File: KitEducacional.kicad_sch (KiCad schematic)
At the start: 23 parts, among them J1 Serial 1, J10 D4, J11 D5, J12 D6, J13 D7, J14 D8, J15 D9, J16 D10, J17 D11, J18 D12, J19 D13, J2 Serial 2, J20 D14, J21 D15, J3 Serial 3, J4 I²C, J5 SPI, J6 D0, J7 D1, J8 D2, J9 D3, U1 ESP32-WROOM-32

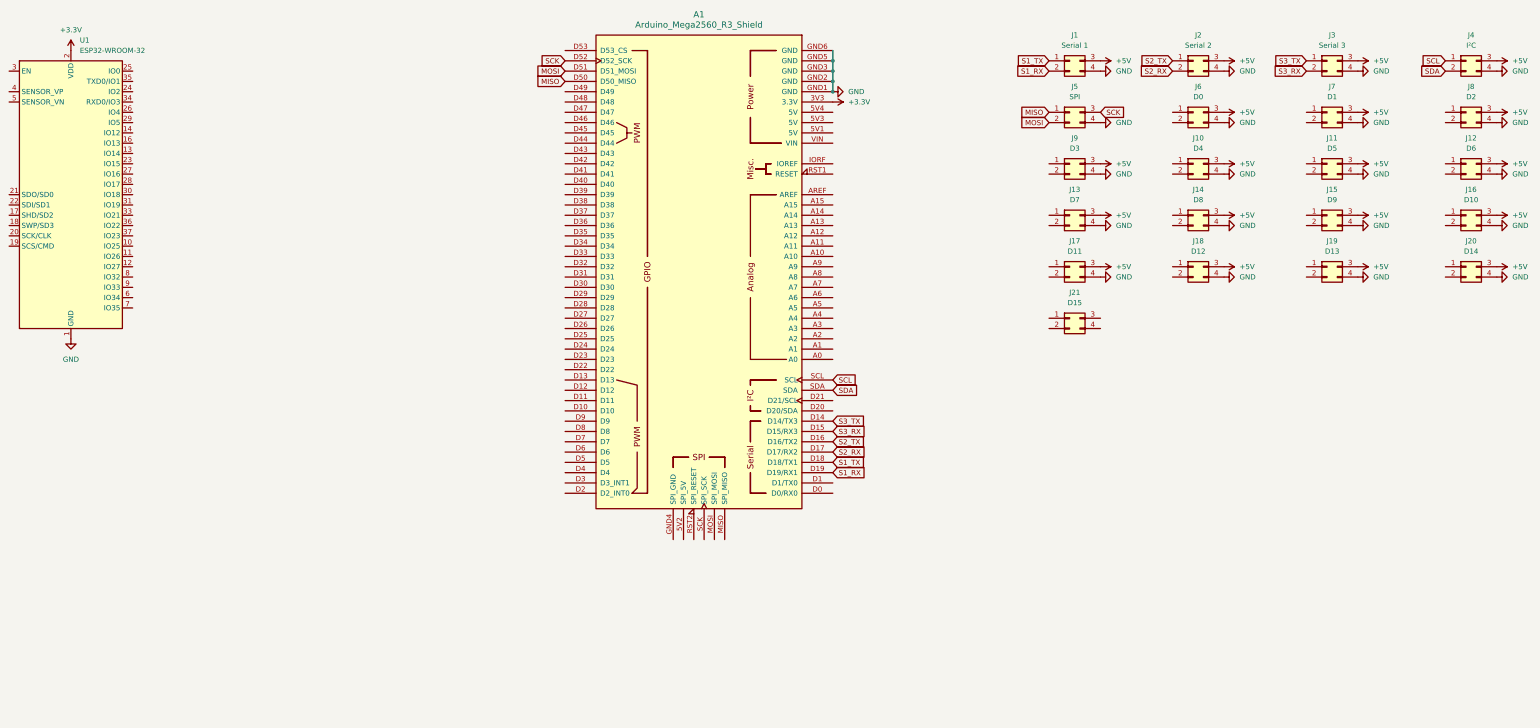
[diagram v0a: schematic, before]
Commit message: add components to board
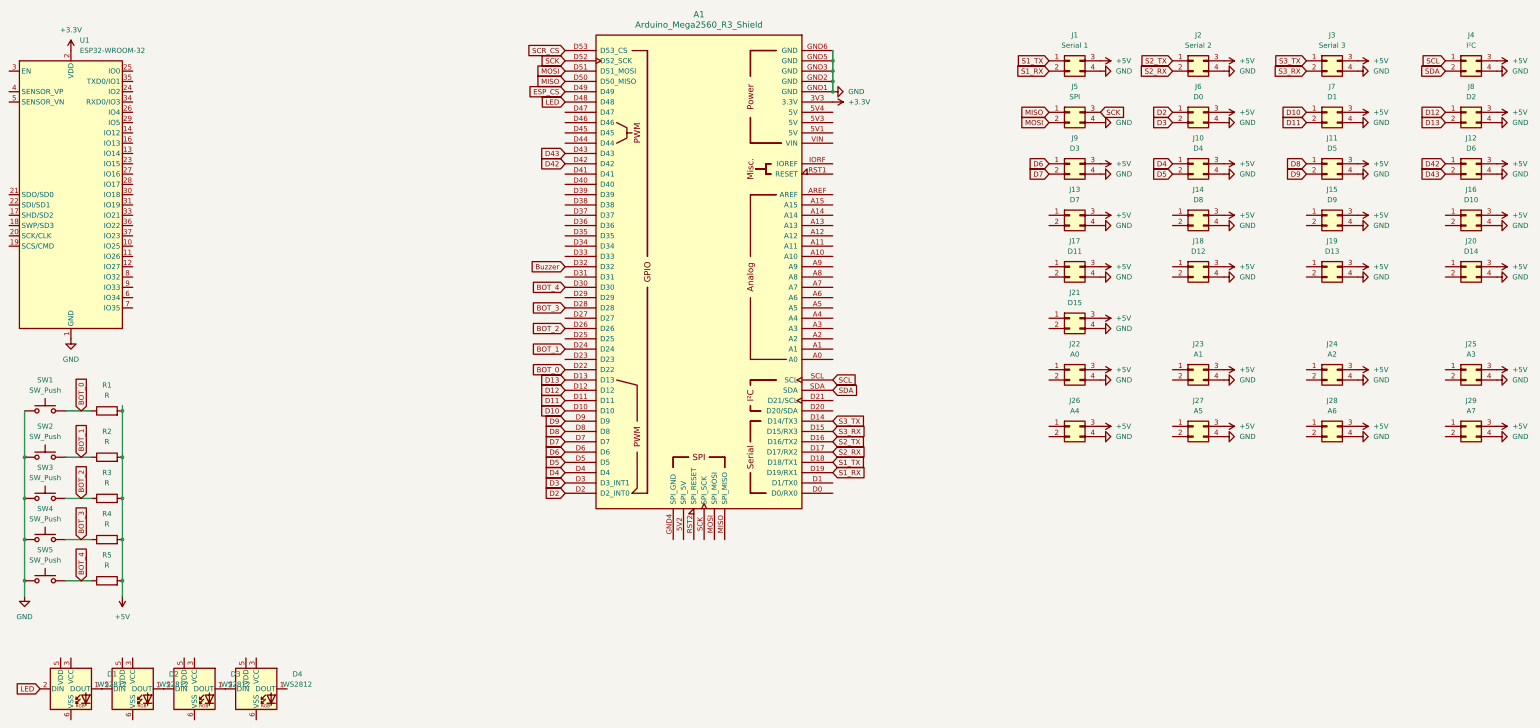
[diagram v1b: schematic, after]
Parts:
- added D1, D2, D3, D4: WS2812, LED_SMD:LED_WS2812_PLCC6_5.0x5.0mm_P1.6mm, symbol LED:WS2812
- added J22: A0, Connector_Molex:Molex_Mini-Fit_Jr_5569-04A2_2x02_P4.20mm_Horizontal, symbol Connector_Generic:Conn_02x02_Top_Bottom
- added J23: A1, Connector_Molex:Molex_Mini-Fit_Jr_5569-04A2_2x02_P4.20mm_Horizontal, symbol Connector_Generic:Conn_02x02_Top_Bottom
- added J24: A2, Connector_Molex:Molex_Mini-Fit_Jr_5569-04A2_2x02_P4.20mm_Horizontal, symbol Connector_Generic:Conn_02x02_Top_Bottom
- added J25: A3, Connector_Molex:Molex_Mini-Fit_Jr_5569-04A2_2x02_P4.20mm_Horizontal, symbol Connector_Generic:Conn_02x02_Top_Bottom
- added J26: A4, Connector_Molex:Molex_Mini-Fit_Jr_5569-04A2_2x02_P4.20mm_Horizontal, symbol Connector_Generic:Conn_02x02_Top_Bottom
- added J27: A5, Connector_Molex:Molex_Mini-Fit_Jr_5569-04A2_2x02_P4.20mm_Horizontal, symbol Connector_Generic:Conn_02x02_Top_Bottom
- added J28: A6, Connector_Molex:Molex_Mini-Fit_Jr_5569-04A2_2x02_P4.20mm_Horizontal, symbol Connector_Generic:Conn_02x02_Top_Bottom
- added J29: A7, Connector_Molex:Molex_Mini-Fit_Jr_5569-04A2_2x02_P4.20mm_Horizontal, symbol Connector_Generic:Conn_02x02_Top_Bottom
- added R1, R2, R3, R4, R5: R, Resistor_SMD:R_0805_2012Metric, symbol Device:R
- added SW1, SW2, SW3, SW4, SW5: SW_Push, Button_Switch_THT:SW_PUSH_6mm, symbol Switch:SW_Push
- J1, J10, J11, J12, J13, J14, J15, J16, J17, J18, J19, J2, J20, J21, J3, J4, J5, J6, J7, J8, J9: footprint Connector_Molex:Molex_Mega-Fit_76825-0004_2x02_P5.70mm_Horizontal -> Connector_Molex:Molex_Mini-Fit_Jr_5569-04A2_2x02_P4.20mm_Horizontal
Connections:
- net +5V: now also J21.3 (Pin_3), J22.3 (Pin_3), J23.3 (Pin_3), J24.3 (Pin_3), J25.3 (Pin_3), J26.3 (Pin_3), J27.3 (Pin_3), J28.3 (Pin_3), J29.3 (Pin_3), R1.2, R2.2, R3.2, R4.2, R5.2
- net GND: now also J21.4 (Pin_4), J22.4 (Pin_4), J23.4 (Pin_4), J24.4 (Pin_4), J25.4 (Pin_4), J26.4 (Pin_4), J27.4 (Pin_4), J28.4 (Pin_4), J29.4 (Pin_4), SW1.1, SW2.1, SW3.1, SW4.1, SW5.1
- net D8: now reaches J11.1 (Pin_1)
- net D8: now also A1.D8
- net D9: now reaches J11.2 (Pin_2)
- net D9: now also A1.D9
- net D4: now reaches J10.1 (Pin_1)
- net D4: now also A1.D4
- net D5: now reaches J10.2 (Pin_2)
- net D5: now also A1.D5
- net D12: now reaches J8.1 (Pin_1)
- net D12: now also A1.D12
- net D13: now reaches J8.2 (Pin_2)
- net D13: now also A1.D13
- net D42: now reaches J12.1 (Pin_1)
- net D42: now also A1.D42
- net D43: now reaches J12.2 (Pin_2)
- net D43: now also A1.D43
- net D10: now reaches A1.D10
- net D10: now also J7.1 (Pin_1)
- net D11: now reaches A1.D11
- net D11: now also J7.2 (Pin_2)
- net D2: now reaches A1.D2 (D2_INT0)
- net D2: now also J6.1 (Pin_1)
- net BOT_0: now reaches A1.D22
- net BOT_0: now also R1.1, SW1.2
- net BOT_1: now reaches A1.D24
- net BOT_1: now also R2.1, SW2.2
- net BOT_2: now reaches A1.D26
- net BOT_2: now also R3.1, SW3.2
- net BOT_3: now reaches A1.D28
- net BOT_3: now also R4.1, SW4.2
- net D3: now reaches A1.D3 (D3_INT1)
- net D3: now also J6.2 (Pin_2)
- net BOT_4: now reaches A1.D30
- net BOT_4: now also R5.1, SW5.2
- net Buzzer: now reaches A1.D32
- net LED: now reaches A1.D48
- net LED: now also D1.2 (DIN)
- net ESP_CS: now reaches A1.D49
- net SCR_CS: now reaches A1.D53 (D53_CS)
- net D6: now reaches A1.D6
- net D6: now also J9.1 (Pin_1)
- net D7: now reaches A1.D7
- net D7: now also J9.2 (Pin_2)
- new net: D3.1 (DOUT), D4.2 (DIN)
- new net: D2.1 (DOUT), D3.2 (DIN)
- new net: D1.1 (DOUT), D2.2 (DIN)

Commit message: go back to molex Nano Fit
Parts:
- J1, J10, J11, J12, J13, J14, J15, J16, J17, J18, J19, J2, J20, J21, J22, J23, J24, J25, J26, J27, J28, J29, J3, J4, J5, J6, J7, J8, J9: footprint Connector_Molex:Molex_Mini-Fit_Jr_5569-04A2_2x02_P4.20mm_Horizontal -> Connector_Molex:Molex_Nano-Fit_105314-xx04_2x02_P2.50mm_Horizontal
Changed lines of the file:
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@@
       (effects (font (size 1.27 1.27)))
     )
-    (property "Footprint" "Connector_Molex:Molex_Mini-Fit_Jr_5569-04A2_2x02_P4.20mm_Horizontal" (at 351.79 53.34 0)
+    (property "Footprint" "Connector_Molex:Molex_Nano-Fit_105314-xx04_2x02_P2.50mm_Horizontal" (at 351.79 53.34 0)
       (effects (font (size 1.27 1.27)) hide)
     )
@@
       (effects (font (size 1.27 1.27)))
     )
-    (property "Footprint" "Connector_Molex:Molex_Mini-Fit_Jr_5569-04A2_2x02_P4.20mm_Horizontal" (at 386.08 66.04 0)
+    (property "Footprint" "Connector_Molex:Molex_Nano-Fit_105314-xx04_2x02_P2.50mm_Horizontal" (at 386.08 66.04 0)
       (effects (font (size 1.27 1.27)) hide)
     )
@@
       (effects (font (size 1.27 1.27)))
     )
-    (property "Footprint" "Connector_Molex:Molex_Mini-Fit_Jr_5569-04A2_2x02_P4.20mm_Horizontal" (at 318.77 78.74 0)
+    (property "Footprint" "Connector_Molex:Molex_Nano-Fit_105314-xx04_2x02_P2.50mm_Horizontal" (at 318.77 78.74 0)
       (effects (font (size 1.27 1.27)) hide)
     )
@@
       (effects (font (size 1.27 1.27)))
     )
-    (property "Footprint" "Connector_Molex:Molex_Mini-Fit_Jr_5569-04A2_2x02_P4.20mm_Horizontal" (at 288.29 27.94 0)
+    (property "Footprint" "Connector_Molex:Molex_Nano-Fit_105314-xx04_2x02_P2.50mm_Horizontal" (at 288.29 27.94 0)
       (effects (font (size 1.27 1.27)) hide)
     )
@@
       (effects (font (size 1.27 1.27)))
     )
-    (property "Footprint" "Connector_Molex:Molex_Mini-Fit_Jr_5569-04A2_2x02_P4.20mm_Horizontal" (at 351.79 78.74 0)
+    (property "Footprint" "Connector_Molex:Molex_Nano-Fit_105314-xx04_2x02_P2.50mm_Horizontal" (at 351.79 78.74 0)
       (effects (font (size 1.27 1.27)) hide)
     )
@@
       (effects (font (size 1.27 1.27)))
     )
-    (property "Footprint" "Connector_Molex:Molex_Mini-Fit_Jr_5569-04A2_2x02_P4.20mm_Horizontal" (at 288.29 91.44 0)
+    (property "Footprint" "Connector_Molex:Molex_Nano-Fit_105314-xx04_2x02_P2.50mm_Horizontal" (at 288.29 91.44 0)
       (effects (font (size 1.27 1.27)) hide)
     )
@@
       (effects (font (size 1.27 1.27)))
     )
-    (property "Footprint" "Connector_Molex:Molex_Mini-Fit_Jr_5569-04A2_2x02_P4.20mm_Horizontal" (at 318.77 53.34 0)
+    (property "Footprint" "Connector_Molex:Molex_Nano-Fit_105314-xx04_2x02_P2.50mm_Horizontal" (at 318.77 53.34 0)
       (effects (font (size 1.27 1.27)) hide)
     )
@@
       (effects (font (size 1.27 1.27)))
     )
-    (property "Footprint" "Connector_Molex:Molex_Mini-Fit_Jr_5569-04A2_2x02_P4.20mm_Horizontal" (at 351.79 27.94 0)
+    (property "Footprint" "Connector_Molex:Molex_Nano-Fit_105314-xx04_2x02_P2.50mm_Horizontal" (at 351.79 27.94 0)
       (effects (font (size 1.27 1.27)) hide)
     )
@@
       (effects (font (size 1.27 1.27)))
     )
-    (property "Footprint" "Connector_Molex:Molex_Mini-Fit_Jr_5569-04A2_2x02_P4.20mm_Horizontal" (at 386.08 40.64 0)
+    (property "Footprint" "Connector_Molex:Molex_Nano-Fit_105314-xx04_2x02_P2.50mm_Horizontal" (at 386.08 40.64 0)
       (effects (font (size 1.27 1.27)) hide)
     )
@@
       (effects (font (size 1.27 1.27)))
     )
-    (property "Footprint" "Connector_Molex:Molex_Mini-Fit_Jr_5569-04A2_2x02_P4.20mm_Horizontal" (at 386.08 118.11 0)
+    (property "Footprint" "Connector_Molex:Molex_Nano-Fit_105314-xx04_2x02_P2.50mm_Horizontal" (at 386.08 118.11 0)
       (effects (font (size 1.27 1.27)) hide)
     )
@@
       (effects (font (size 1.27 1.27)))
     )
-    (property "Footprint" "Connector_Molex:Molex_Mini-Fit_Jr_5569-04A2_2x02_P4.20mm_Horizontal" (at 351.79 104.14 0)
+    (property "Footprint" "Connector_Molex:Molex_Nano-Fit_105314-xx04_2x02_P2.50mm_Horizontal" (at 351.79 104.14 0)
       (effects (font (size 1.27 1.27)) hide)
     )
@@
       (effects (font (size 1.27 1.27)))
     )
-    (property "Footprint" "Connector_Molex:Molex_Mini-Fit_Jr_5569-04A2_2x02_P4.20mm_Horizontal" (at 386.08 53.34 0)
+    (property "Footprint" "Connector_Molex:Molex_Nano-Fit_105314-xx04_2x02_P2.50mm_Horizontal" (at 386.08 53.34 0)
       (effects (font (size 1.27 1.27)) hide)
     )
@@
       (effects (font (size 1.27 1.27)))
     )
-    (property "Footprint" "Connector_Molex:Molex_Mini-Fit_Jr_5569-04A2_2x02_P4.20mm_Horizontal" (at 351.79 66.04 0)
+    (property "Footprint" "Connector_Molex:Molex_Nano-Fit_105314-xx04_2x02_P2.50mm_Horizontal" (at 351.79 66.04 0)
       (effects (font (size 1.27 1.27)) hide)
     )
@@
       (effects (font (size 1.27 1.27)))
     )
-    (property "Footprint" "Connector_Molex:Molex_Mini-Fit_Jr_5569-04A2_2x02_P4.20mm_Horizontal" (at 386.08 104.14 0)
+    (property "Footprint" "Connector_Molex:Molex_Nano-Fit_105314-xx04_2x02_P2.50mm_Horizontal" (at 386.08 104.14 0)
       (effects (font (size 1.27 1.27)) hide)
     )
@@
       (effects (font (size 1.27 1.27)))
     )
-    (property "Footprint" "Connector_Molex:Molex_Mini-Fit_Jr_5569-04A2_2x02_P4.20mm_Horizontal" (at 318.77 104.14 0)
+    (property "Footprint" "Connector_Molex:Molex_Nano-Fit_105314-xx04_2x02_P2.50mm_Horizontal" (at 318.77 104.14 0)
       (effects (font (size 1.27 1.27)) hide)
     )
@@
       (effects (font (size 1.27 1.27)))
     )
-    (property "Footprint" "Connector_Molex:Molex_Mini-Fit_Jr_5569-04A2_2x02_P4.20mm_Horizontal" (at 318.77 66.04 0)
+    (property "Footprint" "Connector_Molex:Molex_Nano-Fit_105314-xx04_2x02_P2.50mm_Horizontal" (at 318.77 66.04 0)
       (effects (font (size 1.27 1.27)) hide)
     )
@@
       (effects (font (size 1.27 1.27)))
     )
-    (property "Footprint" "Connector_Molex:Molex_Mini-Fit_Jr_5569-04A2_2x02_P4.20mm_Horizontal" (at 288.29 40.64 0)
+    (property "Footprint" "Connector_Molex:Molex_Nano-Fit_105314-xx04_2x02_P2.50mm_Horizontal" (at 288.29 40.64 0)
       (effects (font (size 1.27 1.27)) hide)
     )
@@
       (effects (font (size 1.27 1.27)))
     )
-    (property "Footprint" "Connector_Molex:Molex_Mini-Fit_Jr_5569-04A2_2x02_P4.20mm_Horizontal" (at 386.08 78.74 0)
+    (property "Footprint" "Connector_Molex:Molex_Nano-Fit_105314-xx04_2x02_P2.50mm_Horizontal" (at 386.08 78.74 0)
       (effects (font (size 1.27 1.27)) hide)
     )
@@
       (effects (font (size 1.27 1.27)))
     )
-    (property "Footprint" "Connector_Molex:Molex_Mini-Fit_Jr_5569-04A2_2x02_P4.20mm_Horizontal" (at 288.29 53.34 0)
+    (property "Footprint" "Connector_Molex:Molex_Nano-Fit_105314-xx04_2x02_P2.50mm_Horizontal" (at 288.29 53.34 0)
       (effects (font (size 1.27 1.27)) hide)
     )
@@
       (effects (font (size 1.27 1.27)))
     )
-    (property "Footprint" "Connector_Molex:Molex_Mini-Fit_Jr_5569-04A2_2x02_P4.20mm_Horizontal" (at 288.29 66.04 0)
+    (property "Footprint" "Connector_Molex:Molex_Nano-Fit_105314-xx04_2x02_P2.50mm_Horizontal" (at 288.29 66.04 0)
       (effects (font (size 1.27 1.27)) hide)
     )
@@
       (effects (font (size 1.27 1.27)))
     )
-    (property "Footprint" "Connector_Molex:Molex_Mini-Fit_Jr_5569-04A2_2x02_P4.20mm_Horizontal" (at 288.29 78.74 0)
+    (property "Footprint" "Connector_Molex:Molex_Nano-Fit_105314-xx04_2x02_P2.50mm_Horizontal" (at 288.29 78.74 0)
       (effects (font (size 1.27 1.27)) hide)
     )
@@
       (effects (font (size 1.27 1.27)))
     )
-    (property "Footprint" "Connector_Molex:Molex_Mini-Fit_Jr_5569-04A2_2x02_P4.20mm_Horizontal" (at 288.29 118.11 0)
+    (property "Footprint" "Connector_Molex:Molex_Nano-Fit_105314-xx04_2x02_P2.50mm_Horizontal" (at 288.29 118.11 0)
       (effects (font (size 1.27 1.27)) hide)
     )
@@
       (effects (font (size 1.27 1.27)))
     )
-    (property "Footprint" "Connector_Molex:Molex_Mini-Fit_Jr_5569-04A2_2x02_P4.20mm_Horizontal" (at 351.79 40.64 0)
+    (property "Footprint" "Connector_Molex:Molex_Nano-Fit_105314-xx04_2x02_P2.50mm_Horizontal" (at 351.79 40.64 0)
       (effects (font (size 1.27 1.27)) hide)
     )
@@
       (effects (font (size 1.27 1.27)))
     )
-    (property "Footprint" "Connector_Molex:Molex_Mini-Fit_Jr_5569-04A2_2x02_P4.20mm_Horizontal" (at 288.29 104.14 0)
+    (property "Footprint" "Connector_Molex:Molex_Nano-Fit_105314-xx04_2x02_P2.50mm_Horizontal" (at 288.29 104.14 0)
       (effects (font (size 1.27 1.27)) hide)
     )
@@
       (effects (font (size 1.27 1.27)))
     )
-    (property "Footprint" "Connector_Molex:Molex_Mini-Fit_Jr_5569-04A2_2x02_P4.20mm_Horizontal" (at 351.79 118.11 0)
+    (property "Footprint" "Connector_Molex:Molex_Nano-Fit_105314-xx04_2x02_P2.50mm_Horizontal" (at 351.79 118.11 0)
       (effects (font (size 1.27 1.27)) hide)
     )
@@
       (effects (font (size 1.27 1.27)))
     )
-    (property "Footprint" "Connector_Molex:Molex_Mini-Fit_Jr_5569-04A2_2x02_P4.20mm_Horizontal" (at 318.77 27.94 0)
+    (property "Footprint" "Connector_Molex:Molex_Nano-Fit_105314-xx04_2x02_P2.50mm_Horizontal" (at 318.77 27.94 0)
       (effects (font (size 1.27 1.27)) hide)
     )
@@
       (effects (font (size 1.27 1.27)))
     )
-    (property "Footprint" "Connector_Molex:Molex_Mini-Fit_Jr_5569-04A2_2x02_P4.20mm_Horizontal" (at 318.77 118.11 0)
+    (property "Footprint" "Connector_Molex:Molex_Nano-Fit_105314-xx04_2x02_P2.50mm_Horizontal" (at 318.77 118.11 0)
       (effects (font (size 1.27 1.27)) hide)
     )
@@
       (effects (font (size 1.27 1.27)))
     )
-    (property "Footprint" "Connector_Molex:Molex_Mini-Fit_Jr_5569-04A2_2x02_P4.20mm_Horizontal" (at 386.08 27.94 0)
+    (property "Footprint" "Connector_Molex:Molex_Nano-Fit_105314-xx04_2x02_P2.50mm_Horizontal" (at 386.08 27.94 0)
       (effects (font (size 1.27 1.27)) hide)
     )
@@
       (effects (font (size 1.27 1.27)))
     )
-    (property "Footprint" "Connector_Molex:Molex_Mini-Fit_Jr_5569-04A2_2x02_P4.20mm_Horizontal" (at 318.77 40.64 0)
-      (effects (font (size 1.27 1.27)) hide)
-    )
+    (property "Footprint" "Connector_Molex:Molex_Nano-Fit_105314-xx04_2x02_P2.50mm_Horizontal" (at 318.77 40.64 0)
+      (effects (font (size 1.27 1.27)) hide)
+    )

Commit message: goto mini-fit
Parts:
- added BZ1: Buzzer, Buzzer_Beeper:Buzzer_12x9.5RM7.6, symbol Device:Buzzer
- J1, J10, J11, J12, J13, J14, J15, J16, J17, J18, J19, J2, J20, J21, J22, J23, J24, J25, J26, J27, J28, J29, J3, J4, J5, J6, J7, J8, J9: footprint Connector_Molex:Molex_Nano-Fit_105314-xx04_2x02_P2.50mm_Horizontal -> Connector_Molex:Molex_Mini-Fit_Jr_5569-04A2_2x02_P4.20mm_Horizontal
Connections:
- net D35: now reaches J16.1 (Pin_1)
- net D35: now also A1.D35
- net D37: now reaches J16.2 (Pin_2)
- net D37: now also A1.D37
- net D34: now reaches J18.1 (Pin_1)
- net D34: now also A1.D34
- net D36: now reaches J18.2 (Pin_2)
- net D36: now also A1.D36
- net D38: now reaches J19.1 (Pin_1)
- net D38: now also A1.D38
- net D40: now reaches J19.2 (Pin_2)
- net D40: now also A1.D40
- net D44: now reaches J21.1 (Pin_1)
- net D44: now also A1.D44
- net D46: now reaches J21.2 (Pin_2)
- net D46: now also A1.D46
- net D31: now reaches J15.1 (Pin_1)
- net D31: now also A1.D31
- net D33: now reaches J15.2 (Pin_2)
- net D33: now also A1.D33
- net D27: now reaches J14.1 (Pin_1)
- net D27: now also A1.D27
- net D29: now reaches J14.2 (Pin_2)
- net D29: now also A1.D29
- net D23: now reaches A1.D23
- net D23: now also J13.1 (Pin_1)
- net D25: now reaches A1.D25
- net D25: now also J13.2 (Pin_2)
- net D39: now reaches A1.D39
- net D39: now also J17.1 (Pin_1)
- net D41: now reaches A1.D41
- net D41: now also J17.2 (Pin_2)
- net D45: now reaches A1.D45
- net D45: now also J20.1 (Pin_1)
- net D47: now reaches A1.D47
- net D47: now also J20.2 (Pin_2)
